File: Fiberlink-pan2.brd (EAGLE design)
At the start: 50 x 25 mm, 76 parts, among them X1 629105136821

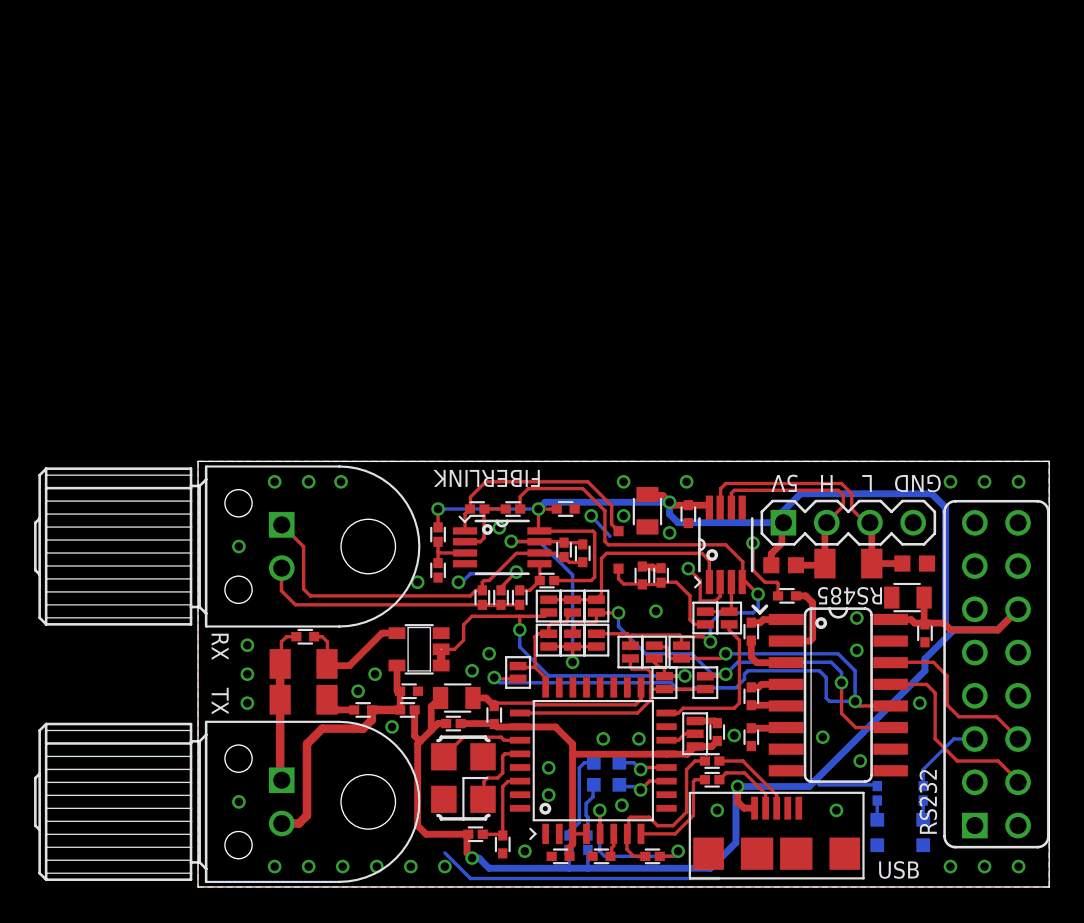
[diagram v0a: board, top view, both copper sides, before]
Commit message: Panelisation added. Corrected drill sizes
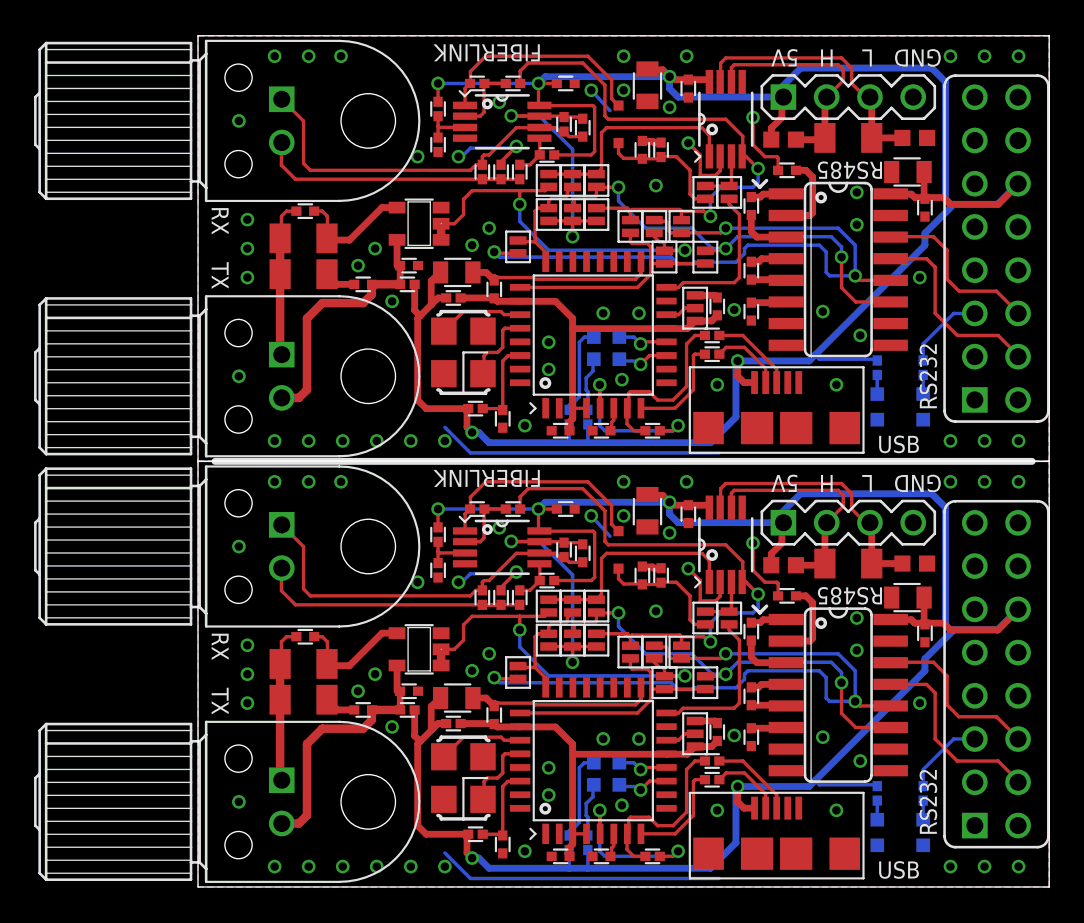
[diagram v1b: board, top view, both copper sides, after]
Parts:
- added C21, C22, C23, C24, C25, C26, C27, C28, C29, C30, C31, C32, C33, C34, C35, C36, C37: (no value), rcl:C0402
- added C38, C39, C40: (no value), rcl:C0805
- added D5: MAX3232CSE, maxim:SO16
- added D6: 74LVC1G08DBV, 74xx-little-us:SOT23-5
- added D7: FT232BL, ftdichip-3:LQFP32
- added D8: SN65HVD3088EDMSOP, OMAT_IC:SOP65P490X110-8N
- added DRILEGEND: (no value), drilegend:DRILEGEND
- added G2: XTAL_3225_SMD, OMAT_IC:X_3225
- added H10, H7, H8, H9: (no value), OMAT_IC:CHIP-LED0603
- added H6: IFE91A, OMAT_IC:IFO-IFX
- added L3, L4, R17, R18, R20, R21, R22, R31, R32, R33, R34, R35, R36, R40, R41, R42, R43, R44, R45, R46: (no value), rcl:R0402_VISHAY
- added N2: MAX412CPAMSOP, OMAT_IC:SOP65P490X110-8N
- added R23, R24, R37: (no value), rcl:R1206
- added R38, R39: (no value), rcl:R0603
- added SJ1, SJ16, SJ18, SJ19, SJ20, SJ21, SJ22, SJ23, SJ24, SJ25, SJ26, SJ27, SJ28, SJ29: (no value), OMAT_IC:SJ-SMALL
- added SJ30: SJ-TRI, OMAT_IC:SJ-SMALL-TRI
- added V3: (no value), diode:SOD323-R
- added V4: IFD91, OMAT_IC:IFO-IFX
- added X4: (no value), OMAT_IC:FE08-2
- added X5: 629105136821, OMAT_IC:629105136821
- added X6: (no value), OMAT_IC:MA04-1
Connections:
- new net +5V1: C22.2, C27.1, C35.2, C38.1, C39.1, C40.1, D5.16, D8.8, L3.1, L4.2, N2.8, R18.2, R33.1, R39.1, R40.1, R43.2, R44.2, R45.1, X4.12, X5.1, X6.1
- new net 485_HIGH1: D8.6, R37.1, R39.2, X6.2
- new net 485_LOW1: D8.7, R37.2, R38.1, X6.3
- new net AVCC1: C30.1, D7.30, R33.2
- new net CARRIER_SENSE1: C36.2, R42.1, SJ28.1, V3.C
- new net FPGADONE1: R46.1, X4.5
- new net G2: D7.27, G2.3
- new net GND1: C22.1, C25.2, C26.2, C27.2, C28.2, C30.2, C31.2, C32.2, C33.2, C34.2, C35.1, C36.1, C37.2, C38.2, C39.2, C40.2, D5.15, D6.3, D7.17, D7.29, D7.31, D7.9, D8.2, D8.5, H10.C, H9.C, N2.4, R20.1, R23.1, R32.2, R38.2, R42.2, SJ30.2, X4.14, X4.16, X4.2, X5.5, X5.Z1, X5.Z2, X5.Z3, X5.Z4, X6.4
- new net N$27: C21.1, N2.6, R17.2, R21.2, V4.1
- new net N$28: R17.1, R20.2, R22.1, V4.2
- new net N$30: N2.5, R18.1, R22.2
- new net N$31: C24.2, D5.5
- new net N$34: C24.1, D5.4
- new net N$35: C23.2, D5.3
- new net N$36: C23.1, D5.1
- new net N$37: C26.1, D5.6
- new net N$38: C25.1, D5.2
- new net N$39: D5.14, X4.6
- new net N$40: C29.1, H6.1, R23.2, R24.2
- new net N$41: C29.2, D6.4, R24.1
- new net N$42: N2.1, R31.1, V3.A
- new net N$43: N2.3, R32.1, R40.2
- new net N$44: R34.1, X5.2
- new net N$45: D7.8, R34.2
- new net N$46: D7.7, R35.2, R36.1
- new net N$47: R35.1, X5.3
- new net N$48: D7.5, R36.2
- new net N$49: D7.28, G2.1
- new net N$50: D5.13, X4.4
- new net N$51: N2.2, R31.2, R41.1
- new net N$52: D7.12, H7.C
- new net N$53: D7.11, H8.C
- new net N$54: H7.A, R43.1
- new net N$55: H8.A, R44.1
- new net N$56: H9.A, R45.2
- new net N$57: H10.A, R46.2
- new net N$58: D7.14, SJ30.3
- new net RXD_1: D5.12, SJ18.2, SJ21.2, SJ26.1
- new net RXD_2: D8.1, SJ22.2, SJ24.2, SJ27.2
- new net RXD_FIBER1: C21.2, N2.7, R21.1, SJ1.1, SJ16.1, SJ23.1
- new net RXD_USB1: D7.24, SJ16.2, SJ21.1, SJ24.1
- new net TXD_1: D5.11, SJ1.2, SJ20.2, SJ27.1
- new net TXD_2: D8.4, R41.2, SJ23.2, SJ25.2, SJ26.2
- new net TXD_FIBER1: D6.1, D6.2, SJ18.1, SJ19.1, SJ22.1
- new net TXD_USB1: D7.25, SJ19.2, SJ20.1, SJ25.1
- new net TXEN_1: D8.3, SJ28.2, SJ29.2
- new net TXEN_USB1: D7.16, SJ29.1
- new net TX_VCC1: C28.1, C37.1, D6.5, H6.2, L4.1
- new net USB3V1: C31.1, D7.6
- new net USBVCC1: C32.1, C33.1, C34.1, D7.13, D7.26, D7.3, D7.4, L3.2, SJ30.1
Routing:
- net +5V1: track 0.00 -> 133.1 mm, vias 0 -> 5
- net GND1: track 0.00 -> 47.1 mm, vias 0 -> 51
- net RXD_1: track 0.00 -> 41.9 mm, vias 0 -> 3
- net TXD_2: track 0.00 -> 32.4 mm, vias 0 -> 2
- net TXD_1: track 0.00 -> 26.3 mm, vias 0 -> 3
- net TXD_FIBER1: track 0.00 -> 23.5 mm, vias 0 -> 2
- net USBVCC1: track 0.00 -> 23.5 mm
- net N$27: track 0.00 -> 22.4 mm
- net RXD_FIBER1: track 0.00 -> 17.5 mm, vias 0 -> 2
- net N$28: track 0.00 -> 16.8 mm
- net 485_LOW1: track 0.00 -> 15.7 mm
- net TX_VCC1: track 0.00 -> 15.3 mm
- net TXD_USB1: track 0.00 -> 14.7 mm
- net 485_HIGH1: track 0.00 -> 13.8 mm
- net RXD_2: track 0.00 -> 13.2 mm
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- added copper zone on layer 1, net GND1
- added copper zone on layer 16, net GND1
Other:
- board size 50 x 25 mm -> 50 x 50 mm
